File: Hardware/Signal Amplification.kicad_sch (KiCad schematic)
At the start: 18 parts, among them U1 Opamp_Quad

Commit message: PCB is done???
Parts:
- C5: footprint (none) -> Capacitor_SMD:C_0402_1005Metric_Pad0.74x0.62mm_HandSolder
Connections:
- net +3V3: now also U1.6 (-)
- net GND: now also C5.2, U1.5 (+)
- net OUT REF_Half3V3: no longer C5.2
- no-connect marks 0 -> 1
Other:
- moved on the sheet: C6, R8, U1B
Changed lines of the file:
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@@
 	)
 	(junction
-		(at 162.56 134.62)
+		(at 162.56 124.46)
 		(diameter 0)
 		(color 0 0 0 0)
@@
 	)
 	(junction
-		(at 142.24 134.62)
+		(at 142.24 124.46)
 		(diameter 0)
 		(color 0 0 0 0)
@@
 		(color 0 0 0 0)
 	)
+	(no_connect
+		(at 234.95 82.55)
+	)
 	(wire
 		(pts
@@
 	(wire
 		(pts
+			(xy 214.63 85.09) (xy 219.71 85.09)
+		)
+		(stroke
+			(width 0)
+			(type default)
+		)
+	)
+	(wire
+		(pts
 			(xy 142.24 97.79) (xy 142.24 113.03)
 		)
@@
 	(wire
 		(pts
+			(xy 214.63 77.47) (xy 214.63 85.09)
+		)
+		(stroke
+			(width 0)
+			(type default)
+		)
+	)
+	(wire
+		(pts
 			(xy 208.28 60.96) (xy 201.93 60.96)
 		)
@@
 	(wire
 		(pts
+			(xy 217.17 87.63) (xy 217.17 80.01)
+		)
+		(stroke
+			(width 0)
+			(type default)
+		)
+	)
+	(wire
+		(pts
 			(xy 100.33 62.23) (xy 100.33 69.85)
 		)
@@
 	(wire
 		(pts
-			(xy 162.56 134.62) (xy 153.67 134.62)
+			(xy 162.56 124.46) (xy 153.67 124.46)
 		)
 		(stroke
@@
 	(wire
 		(pts
+			(xy 217.17 80.01) (xy 219.71 80.01)
+		)
+		(stroke
+			(width 0)
+			(type default)
+		)
+	)
+	(wire
+		(pts
 			(xy 162.56 115.57) (xy 173.99 115.57)
 		)
@@
 	(wire
 		(pts
-			(xy 162.56 139.7) (xy 162.56 134.62)
+			(xy 162.56 129.54) (xy 162.56 124.46)
 		)
 		(stroke
@@
 	(wire
 		(pts
-			(xy 153.67 139.7) (xy 162.56 139.7)
+			(xy 153.67 129.54) (xy 162.56 129.54)
 		)
 		(stroke
@@
 	(wire
 		(pts
-			(xy 146.05 139.7) (xy 142.24 139.7)
+			(xy 146.05 129.54) (xy 142.24 129.54)
 		)
 		(stroke
@@
 	(wire
 		(pts
-			(xy 146.05 134.62) (xy 142.24 134.62)
+			(xy 146.05 124.46) (xy 142.24 124.46)
 		)
 		(stroke
@@
 	(wire
 		(pts
-			(xy 149.86 123.19) (xy 149.86 125.73)
-		)
-		(stroke
-			(width 0)
-			(type default)
-		)
-	)
-	(wire
-		(pts
 			(xy 189.23 57.15) (xy 180.34 57.15)
 		)
@@
 	(wire
 		(pts
-			(xy 142.24 134.62) (xy 142.24 118.11)
+			(xy 142.24 124.46) (xy 142.24 118.11)
 		)
 		(stroke
@@
 	(wire
 		(pts
-			(xy 149.86 105.41) (xy 149.86 107.95)
-		)
-		(stroke
-			(width 0)
-			(type default)
-		)
-	)
-	(wire
-		(pts
-			(xy 162.56 115.57) (xy 162.56 134.62)
-		)
-		(stroke
-			(width 0)
-			(type default)
-		)
-	)
-	(wire
-		(pts
-			(xy 142.24 139.7) (xy 142.24 134.62)
+			(xy 162.56 115.57) (xy 162.56 124.46)
+		)
+		(stroke
+			(width 0)
+			(type default)
+		)
+	)
+	(wire
+		(pts
+			(xy 142.24 129.54) (xy 142.24 124.46)
 		)
 		(stroke
@@
 				(size 1.27 1.27)
 			)
+		)
+	)
+	(hierarchical_label "GND"
+		(shape input)
+		(at 217.17 87.63 270)
+		(effects
+			(font
+				(size 1.27 1.27)
+			)
+			(justify right)
 		)
 	)
@@
 		)
 	)
+	(hierarchical_label "+3V3"
+		(shape input)
+		(at 214.63 77.47 90)
+		(effects
+			(font
+				(size 1.27 1.27)
+			)
+			(justify left)
+		)
+	)
 	(hierarchical_label "OUT REF_Half3V3"
 		(shape input)
@@
 	(hierarchical_label "+3V3"
 		(shape input)
-		(at 149.86 105.41 90)
-		(effects
-			(font
-				(size 1.27 1.27)
-			)
-			(justify left)
-		)
-	)
-	(hierarchical_label "+3V3"
-		(shape input)
 		(at 92.71 22.86 90)
 		(effects
@@
 			)
 			(justify left)
+		)
+	)
+	(hierarchical_label "GND"
+		(shape input)
+		(at 185.42 135.89 270)
+		(effects
+			(font
+				(size 1.27 1.27)
+			)
+			(justify right)
 		)
 	)
@@
 		)
 	)
-	(hierarchical_label "GND"
-		(shape input)
-		(at 149.86 125.73 270)
-		(effects
-			(font
-				(size 1.27 1.27)
-			)
-			(justify right)
-		)
-	)
 	(hierarchical_label "+3V3"
 		(shape input)
@@
 		(shape input)
 		(at 134.62 97.79 180)
-		(effects
-			(font
-				(size 1.27 1.27)
-			)
-			(justify right)
-		)
-	)
-	(hierarchical_label "OUT REF_Half3V3"
-		(shape input)
-		(at 185.42 135.89 270)
 		(effects
 			(font
@@
 	(symbol
 		(lib_id "Device:R")
-		(at 149.86 134.62 90)
+		(at 149.86 124.46 90)
 		(unit 1)
 		(exclude_from_sim no)
@@
 		(dnp no)
 		(property "Reference" "R8"
-			(at 148.59 134.62 90)
+			(at 148.59 124.46 90)
 			(effects
 				(font
@@
 		)
 		(property "Value" "470kΩ"
-			(at 150.368 132.334 90)
+			(at 150.368 122.174 90)
 			(effects
 				(font
@@
 		)
 		(property "Footprint" "Resistor_SMD:R_0402_1005Metric_Pad0.72x0.64mm_HandSolder"
-			(at 149.86 136.398 90)
+			(at 149.86 126.238 90)
 			(effects
 				(font
@@
 		)
 		(property "Datasheet" "~"
-			(at 149.86 134.62 0)
+			(at 149.86 124.46 0)
 			(effects
 				(font
@@
 		)
 		(property "Description" "Resistor"
-			(at 149.86 134.62 0)
+			(at 149.86 124.46 0)
 			(effects
 				(font
@@
 			)
 		)
-		(property "Footprint" ""
+		(property "Footprint" "Capacitor_SMD:C_0402_1005Metric_Pad0.74x0.62mm_HandSolder"
 			(at 186.3852 130.81 0)
 			(effects
@@
 	(symbol
 		(lib_id "Device:Opamp_Quad")
-		(at 220.98 140.97 0)
+		(at 227.33 82.55 0)
 		(unit 2)
 		(exclude_from_sim no)
@@
 		(fields_autoplaced yes)
 		(property "Reference" "U1"
-			(at 220.98 130.81 0)
+			(at 227.33 72.39 0)
 			(effects
 				(font
@@
 		)
 		(property "Value" "Opamp_Quad"
-			(at 220.98 133.35 0)
+			(at 227.33 74.93 0)
 			(effects
 				(font
@@
 		)
 		(property "Footprint" "Package_SO:TSSOP-14_4.4x5mm_P0.65mm"
-			(at 220.98 140.97 0)
+			(at 227.33 82.55 0)
 			(effects
 				(font
@@
 		)
 		(property "Datasheet" "~"
-			(at 220.98 140.97 0)
+			(at 227.33 82.55 0)
 			(effects
 				(font
@@
 		)
 		(property "Description" "Quad operational amplifier"
-			(at 220.98 140.97 0)
+			(at 227.33 82.55 0)
 			(effects
 				(font
@@
 		)
 		(property "Sim.Library" "${KICAD7_SYMBOL_DIR}/Simulation_SPICE.sp"
-			(at 220.98 140.97 0)
+			(at 227.33 82.55 0)
 			(effects
 				(font
@@
 		)
 		(property "Sim.Name" "kicad_builtin_opamp_quad"
-			(at 220.98 140.97 0)
+			(at 227.33 82.55 0)
 			(effects
 				(font
@@
 		)
 		(property "Sim.Device" "SUBCKT"
-			(at 220.98 140.97 0)
+			(at 227.33 82.55 0)
 			(effects
 				(font
@@
 		)
 		(property "Sim.Pins" "1=out1 2=in1- 3=in1+ 4=vcc 5=in2+ 6=in2- 7=out2 8=out3 9=in3- 10=in3+ 11=vee 12=in4+ 13=in4- 14=out4"
-			(at 220.98 140.97 0)
+			(at 227.33 82.55 0)
 			(effects
 				(font
@@
 	(symbol
 		(lib_id "Device:C")
-		(at 149.86 139.7 90)
+		(at 149.86 129.54 90)
 		(unit 1)
 		(exclude_from_sim no)
@@
 		(dnp no)
 		(property "Reference" "C6"
-			(at 152.4 138.43 90)
+			(at 152.4 128.27 90)
 			(effects
 				(font
@@
 		)
 		(property "Value" "68pF"
-			(at 153.67 140.97 90)
+			(at 153.67 130.81 90)
 			(effects
 				(font
@@
 		)
 		(property "Footprint" "Capacitor_SMD:C_0603_1608Metric_Pad1.08x0.95mm_HandSolder"
-			(at 153.67 138.7348 0)
+			(at 153.67 128.5748 0)
 			(effects
 				(font
@@
 		)
 		(property "Datasheet" "~"
-			(at 149.86 139.7 0)
+			(at 149.86 129.54 0)
 			(effects
 				(font
@@
 		)
 		(property "Description" "Unpolarized capacitor"
-			(at 149.86 139.7 0)
-			(effects
-				(font
+			(at 149.86 129.54 0)
+			(effects
+				(font

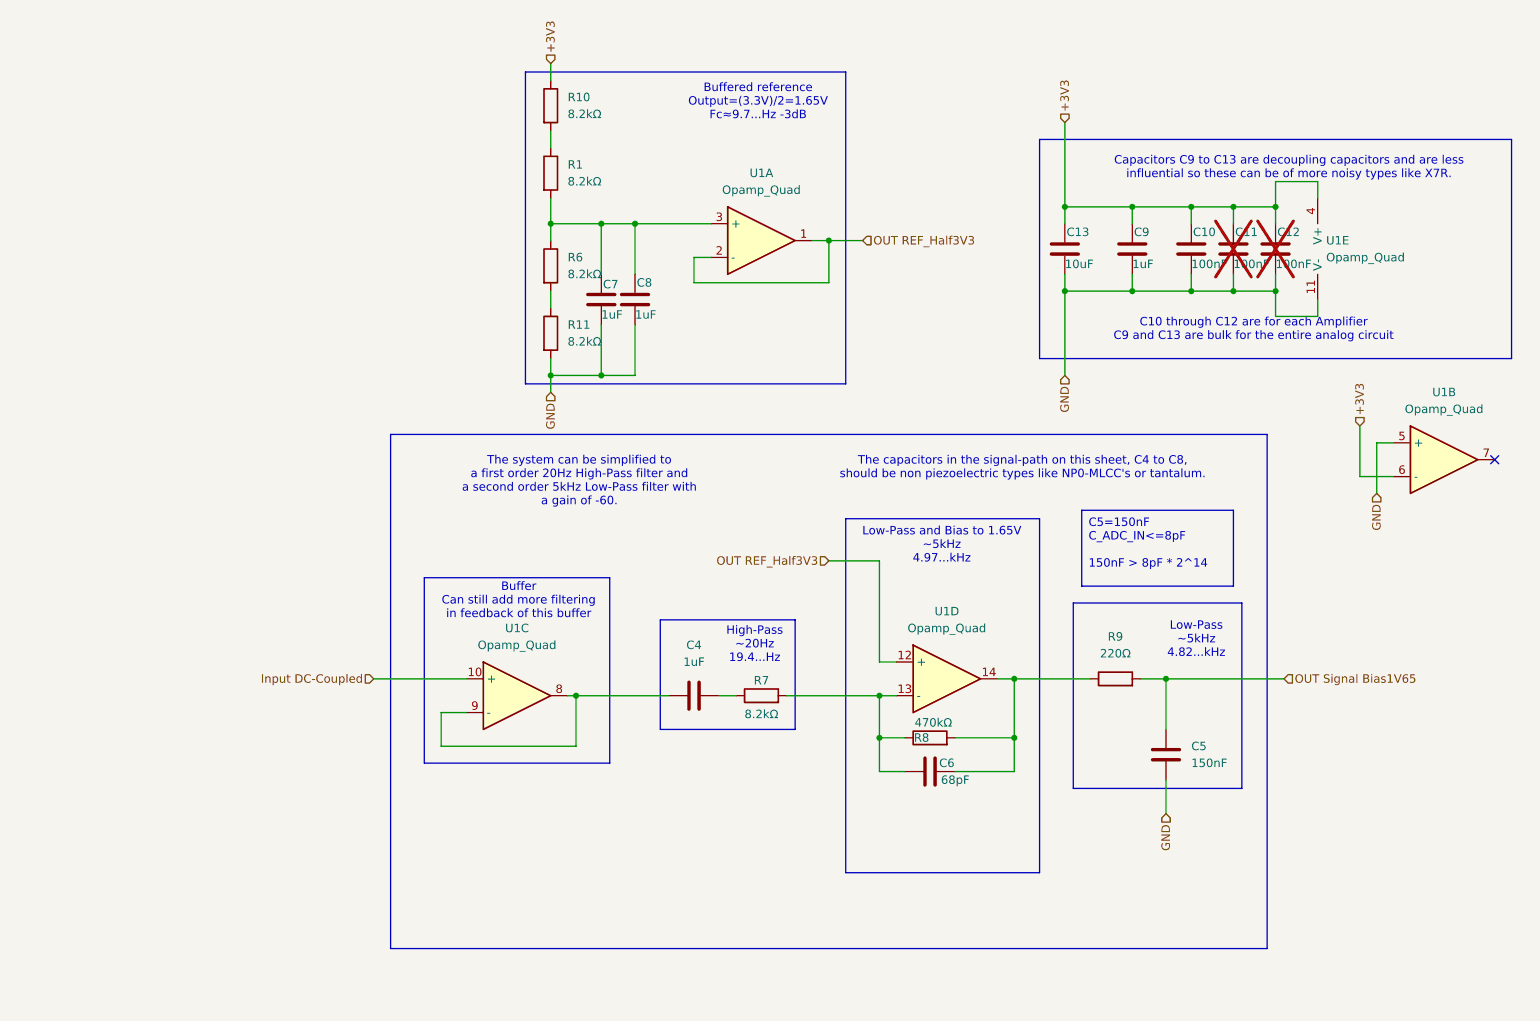
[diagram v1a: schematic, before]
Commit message: Added headphone output to schematic
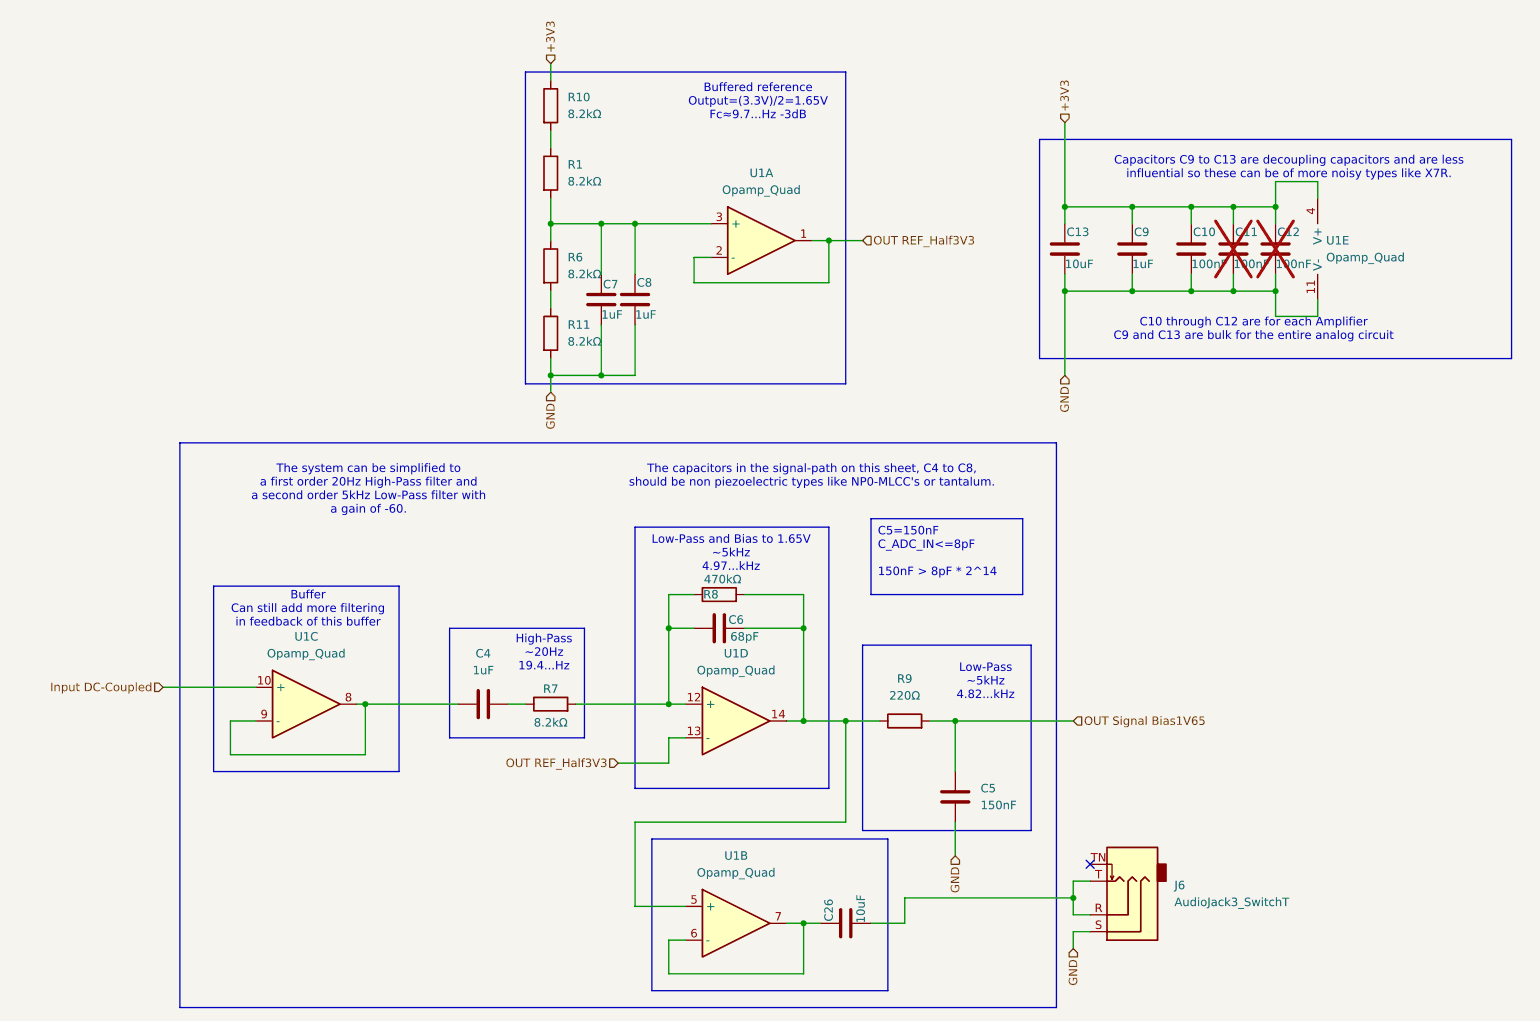
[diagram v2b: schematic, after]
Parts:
- added C26: 10uF, Capacitor_SMD:C_0805_2012Metric_Pad1.18x1.45mm_HandSolder, symbol Device:C
- added J6: AudioJack3_SwitchT, symbol Connector_Audio:AudioJack3_SwitchT
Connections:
- net +3V3: no longer U1.6 (-)
- net GND: now also J6.S; no longer U1.5 (+)
- net OUT REF_Half3V3: now also U1.13 (-); no longer U1.12 (+)
- net at C6.2, R8.2, R9.1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: now also U1.5 (+)
- net at C6.1, R7.2, R8.1: now also U1.12 (+); no longer U1.13 (-)
- net at U1.7: now also U1.6 (-), C26.1
- new net: C26.2, J6.R, J6.T
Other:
- moved on the sheet: C4, C5, C6, R7, R8, R9, U1B, U1C

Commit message: added headphone jack footprint, SJ-3524-SMT
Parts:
- J6: footprint (none) -> Connector_Audio:Jack_3.5mm_CUI_SJ-3524-SMT_Horizontal
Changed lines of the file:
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@@
 			)
 		)
-		(property "Footprint" ""
+		(property "Footprint" "Connector_Audio:Jack_3.5mm_CUI_SJ-3524-SMT_Horizontal"
 			(at 179.07 151.13 0)
 			(effects

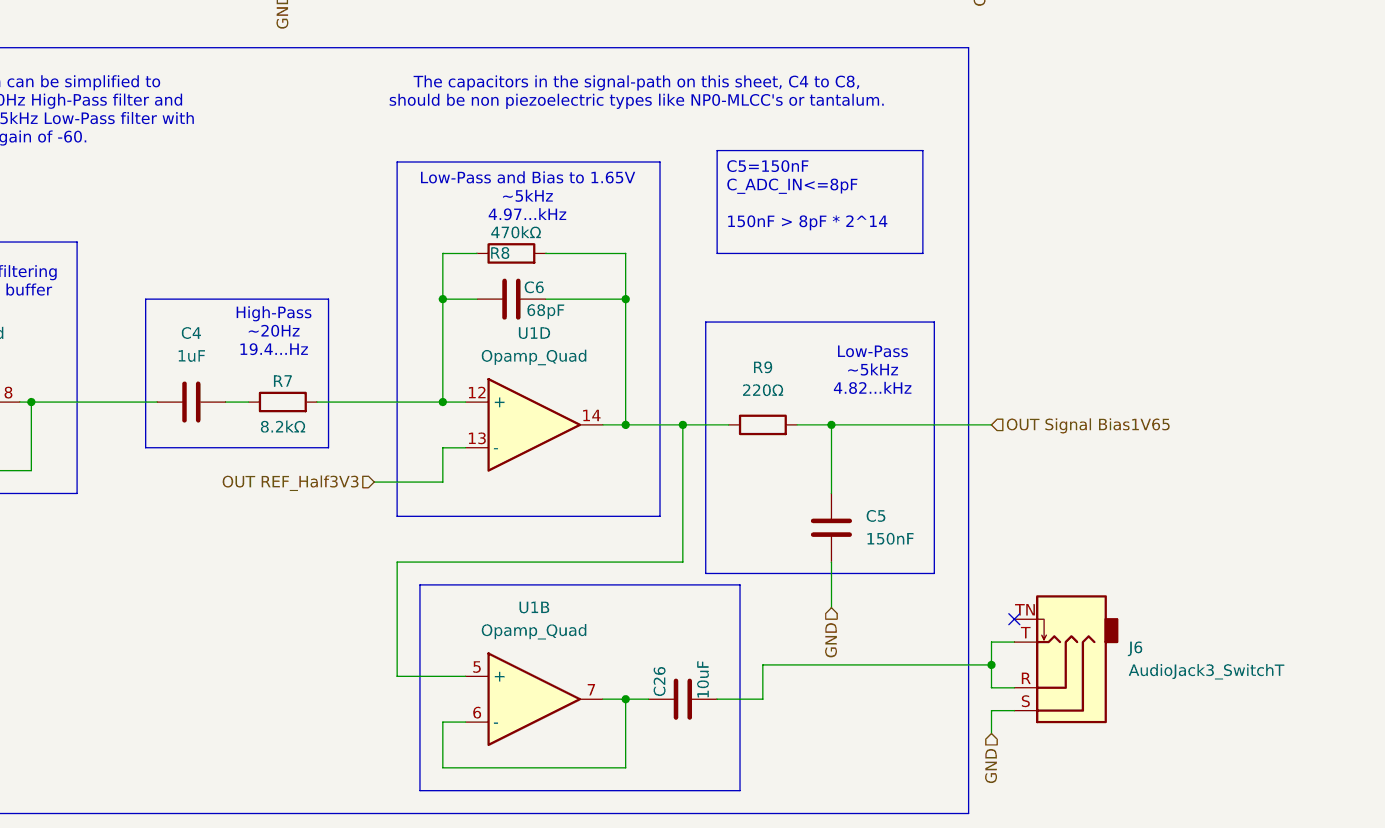
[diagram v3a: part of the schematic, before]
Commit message: The inverting opamp was fixed wrong now it's fixed in the schematic
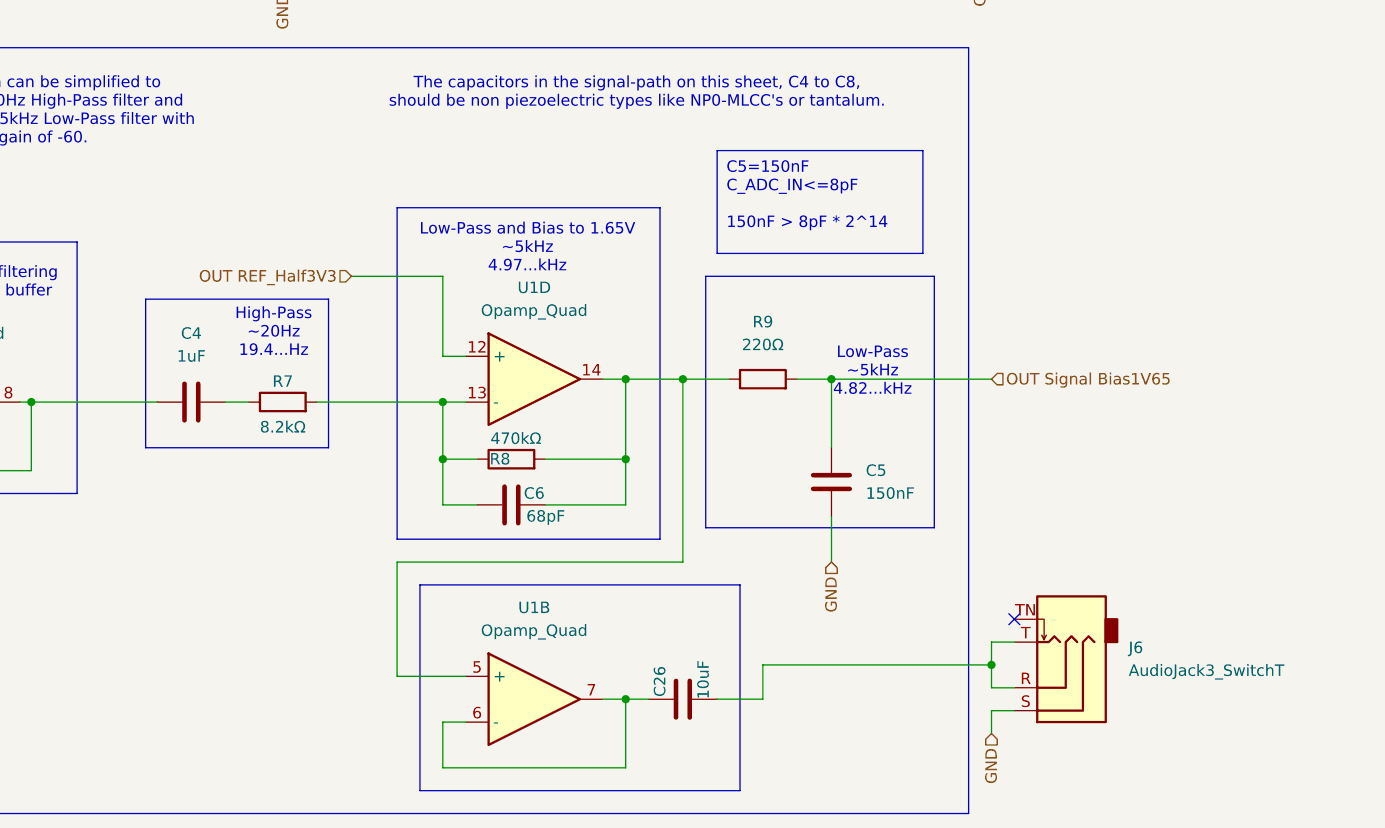
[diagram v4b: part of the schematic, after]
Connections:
- net OUT REF_Half3V3: now also U1.12 (+); no longer U1.13 (-)
- net at C6.1, R7.2, R8.1: now also U1.13 (-); no longer U1.12 (+)
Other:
- moved on the sheet: C5, R9, U1D

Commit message: Inverting opamp is now also fixed on the PCB
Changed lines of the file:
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@@
 	(text "Low-Pass\n~5kHz\n4.82...kHz"
 		(exclude_from_sim no)
-		(at 158.242 116.078 0)
+		(at 158.496 110.236 0)
 		(effects
 			(font
